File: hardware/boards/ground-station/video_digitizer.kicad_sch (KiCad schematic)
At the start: 9 parts, among them Y601 28.63636MHz

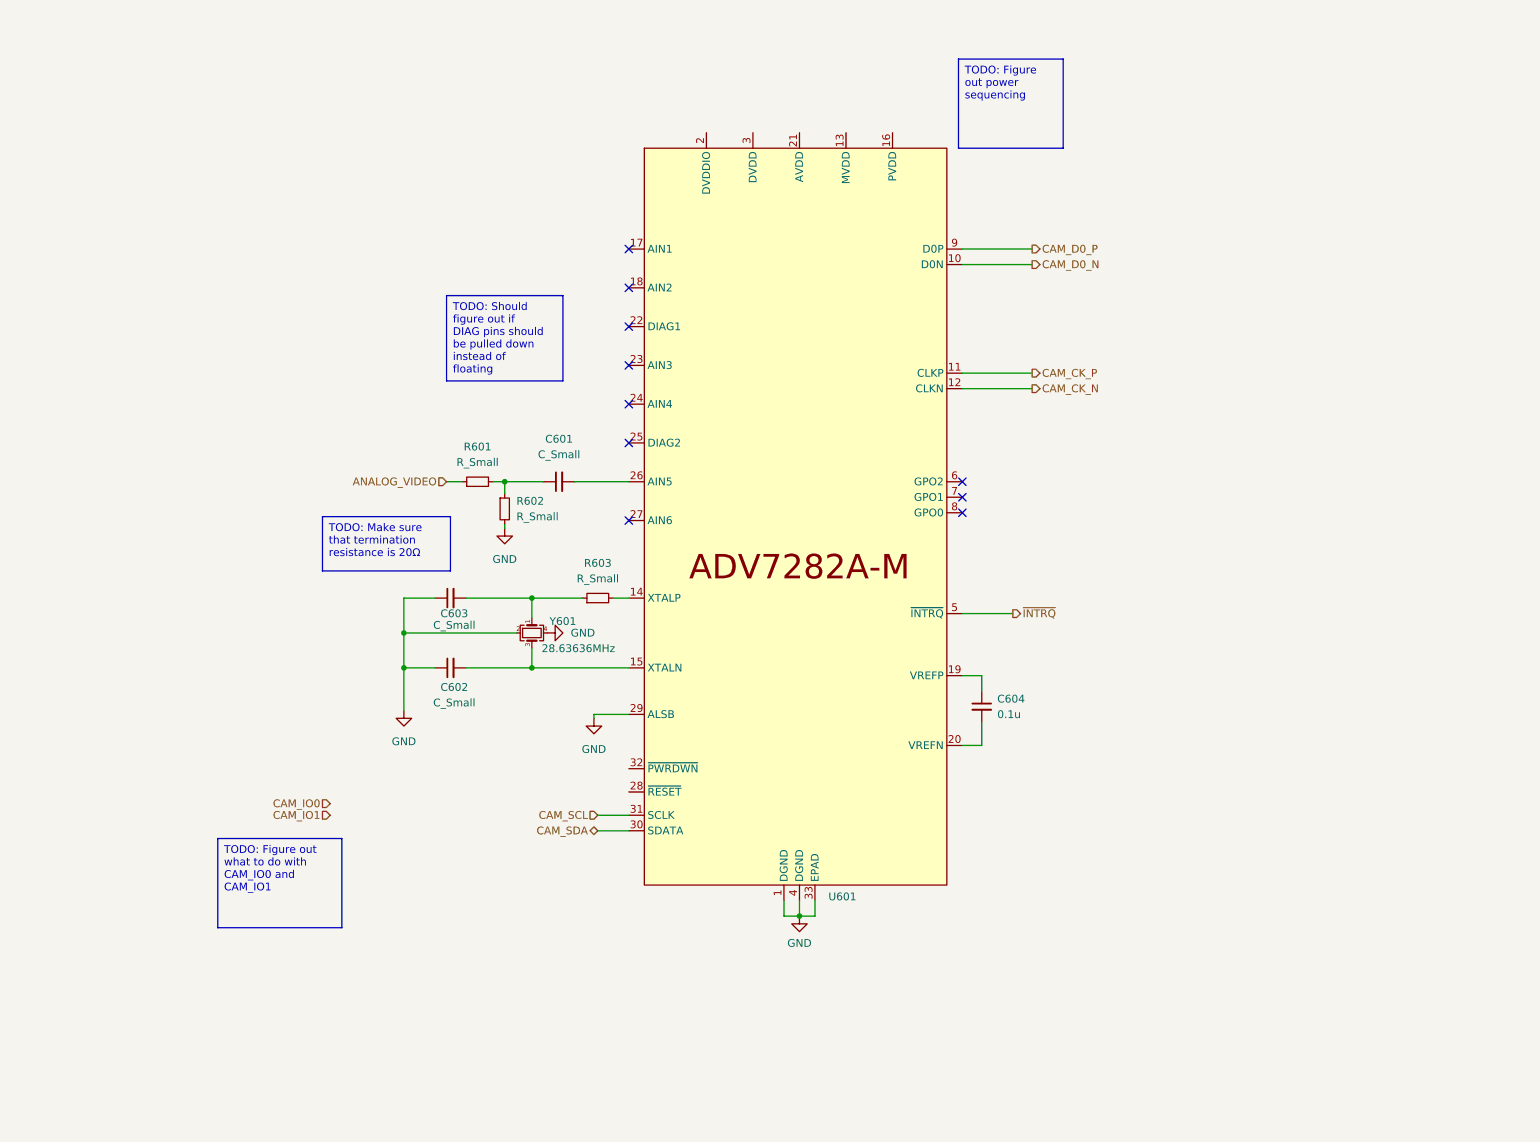
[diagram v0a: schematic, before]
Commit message: Added power supplies to digitizer IC
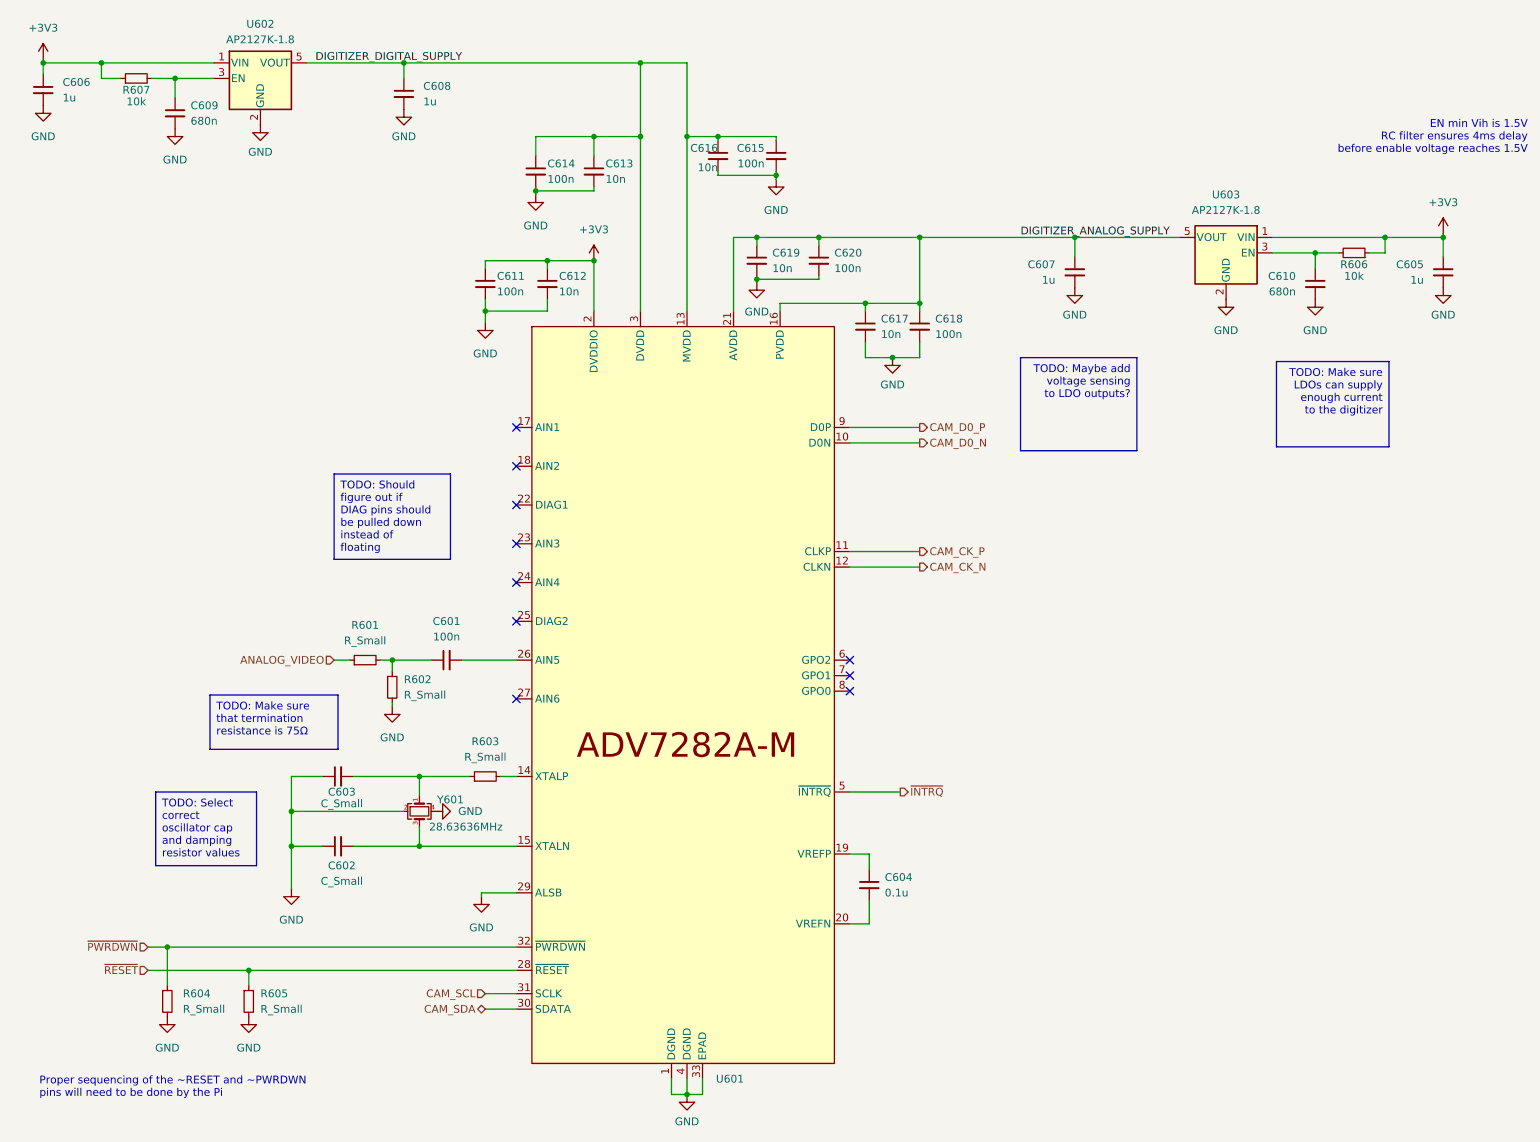
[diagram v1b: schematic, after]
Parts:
- added C605, C606, C607, C608: 1u, symbol Device:C_Small
- added C609, C610: 680n, symbol Device:C_Small
- added C611, C614, C615, C618, C620: 100n, symbol Device:C_Small
- added C612, C613, C616, C617, C619: 10n, symbol Device:C_Small
- added R604, R605: R_Small, symbol Device:R_Small
- added R606, R607: 10k, symbol Device:R_Small
- added U602, U603: AP2127K-1.8, Package_TO_SOT_SMD:SOT-23-5, symbol Regulator_Linear:AP2127K-1.8
- C601: value C_Small -> 100n
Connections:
- net GND: now also C605.2, C606.2, C607.2, C608.2, C609.2, C610.2, C611.2, C612.2, C613.2, C614.2, C615.2, C616.2, C617.2, C618.2, C619.2, C620.2, R604.2, R605.2, U602.2 (GND), U603.2 (GND)
- net DIGITIZER_DIGITAL_SUPPLY: now reaches U601.13 (MVDD)
- net DIGITIZER_DIGITAL_SUPPLY: now also U601.3 (DVDD), C608.1, C613.1, C614.1, C615.1, C616.1, U602.5 (VOUT)
- net DIGITIZER_ANALOG_SUPPLY: now reaches U601.16 (PVDD)
- net DIGITIZER_ANALOG_SUPPLY: now also U601.21 (AVDD), C607.1, C617.1, C618.1, C619.1, C620.1, U603.5 (VOUT)
- net +3V3: now reaches U601.2 (DVDDIO)
- net +3V3: now also C605.1, C606.1, C611.1, C612.1, R606.1, R607.1, U602.1 (VIN), U603.1 (VIN)
- net ~{RESET}: now reaches U601.28 (~{RESET})
- net ~{RESET}: now also R605.1
- net ~{PWRDWN}: now reaches U601.32 (~{PWRDWN})
- net ~{PWRDWN}: now also R604.1
- new net: C610.1, R606.2, U603.3 (EN)
- new net: C609.1, R607.2, U602.3 (EN)
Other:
- note added: "EN min Vih is 1.5V RC filter ensures 4ms delay before enable voltage reaches 1.5V"
- note added: "Proper sequencing of the ~RESET and ~PWRDWN pins will need to be done by the Pi"
- moved on the sheet: C601, C602, C603, C604, R601, R602, R603, Y601

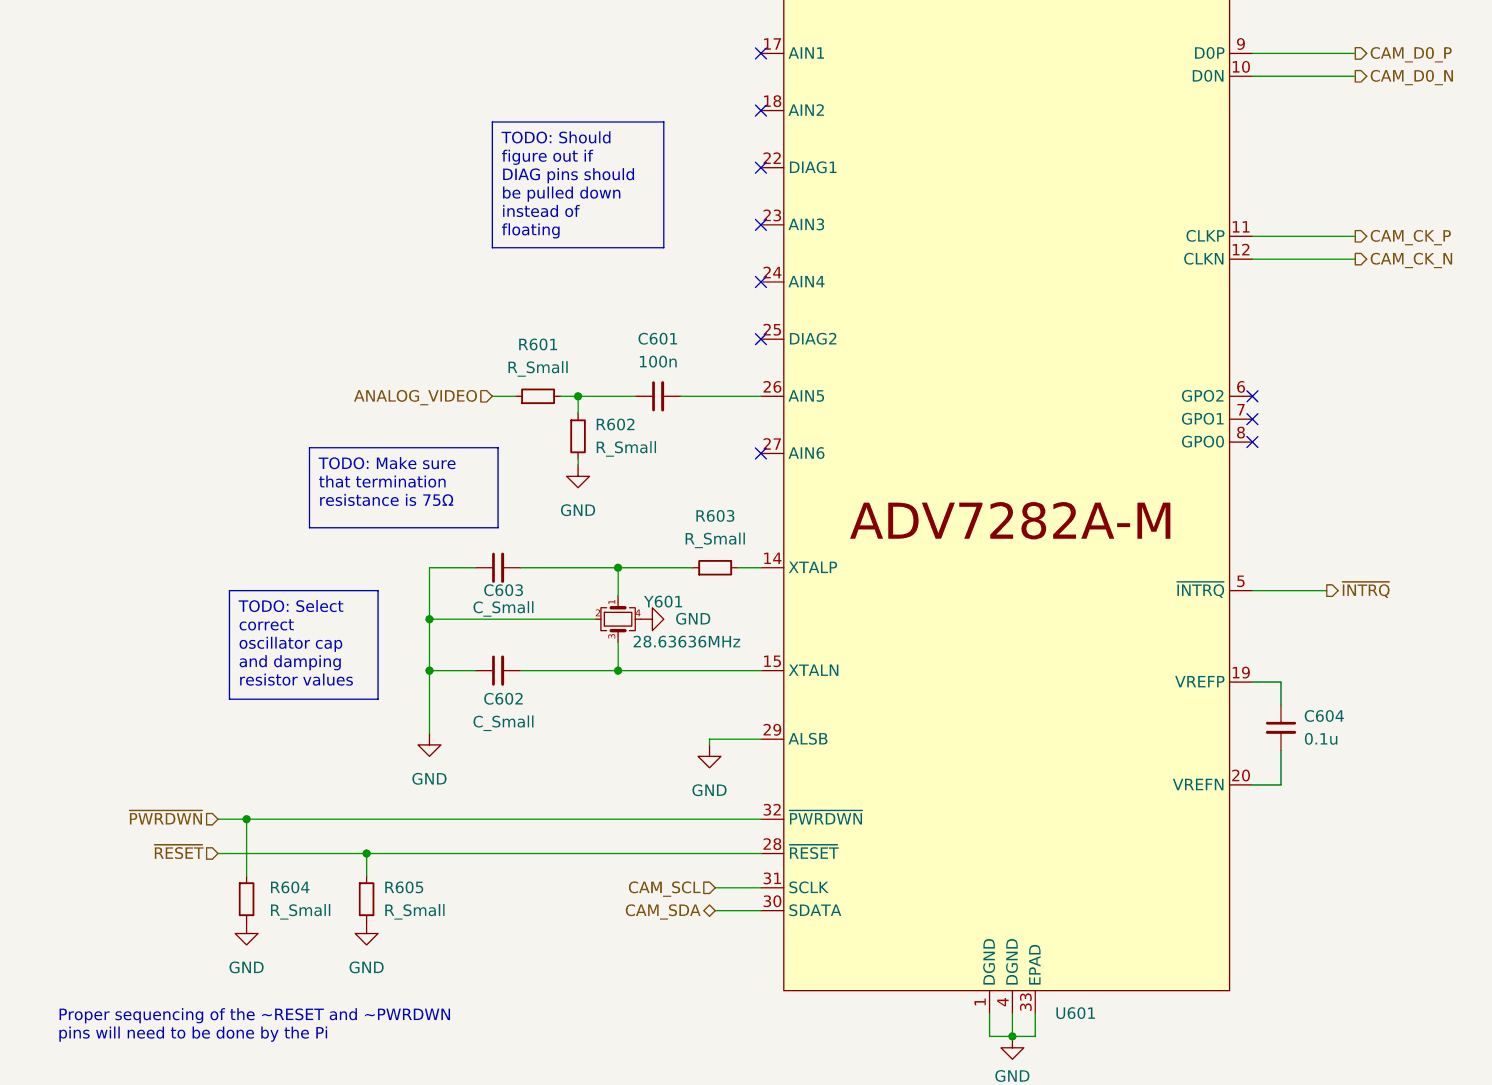
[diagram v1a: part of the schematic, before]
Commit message: Added oscillator to video digitizer
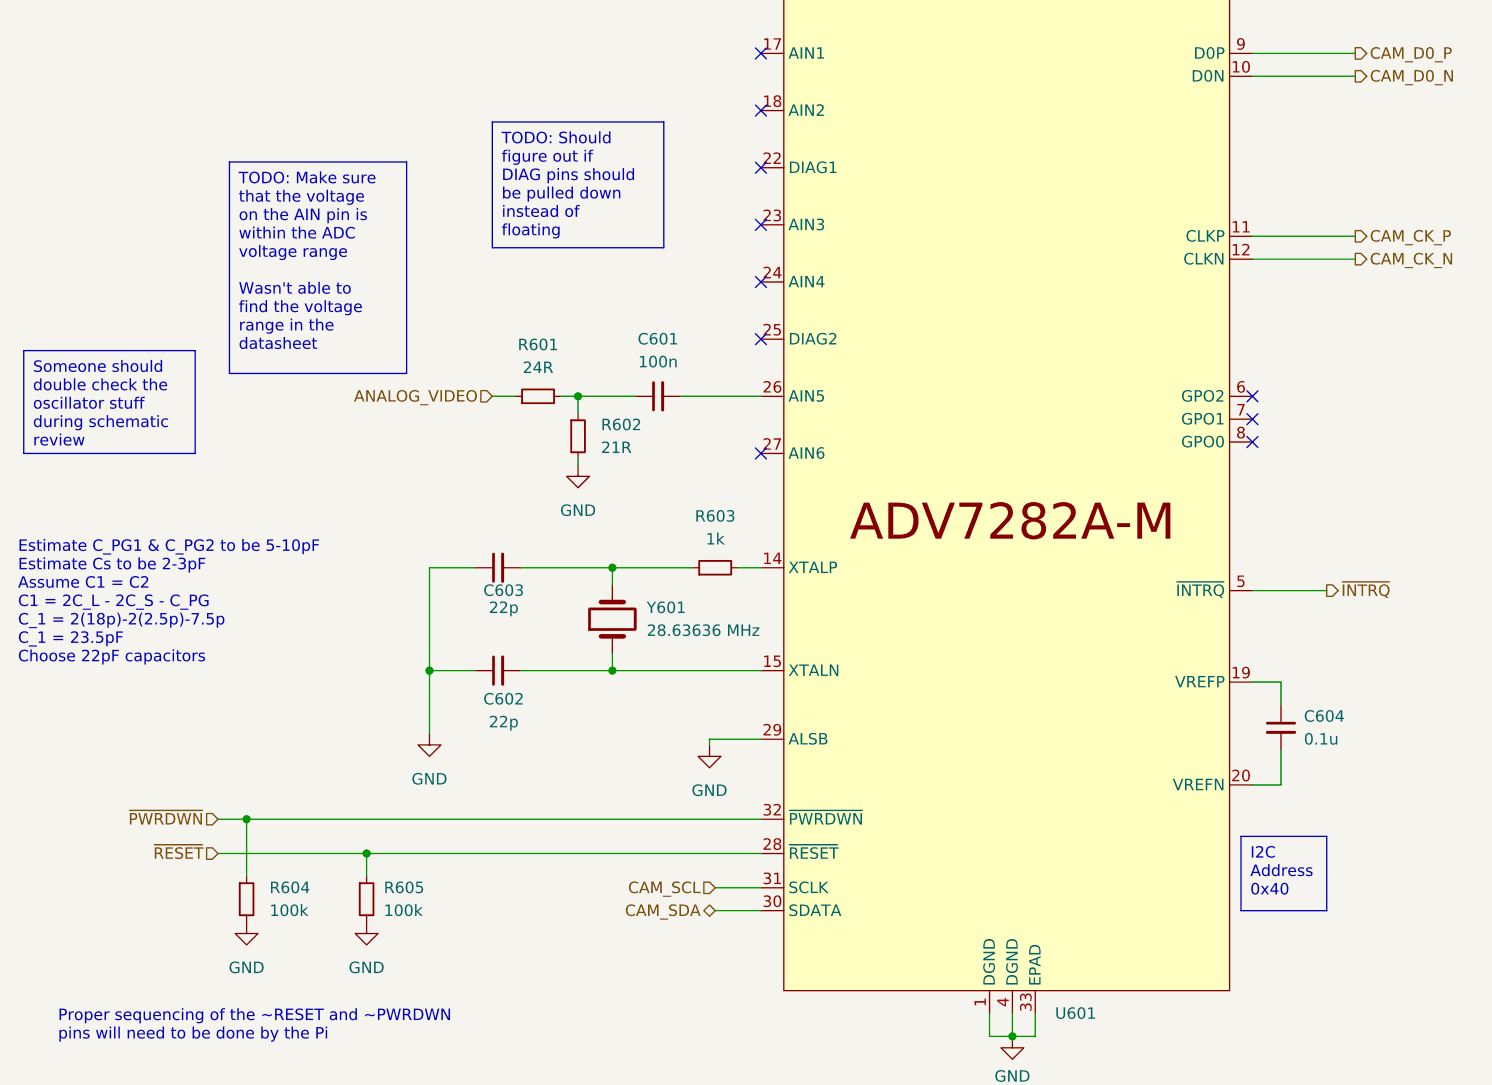
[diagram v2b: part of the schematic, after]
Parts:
- removed Y601: 28.63636MHz, symbol Device:Crystal_GND24_Small
- added Y601: 28.63636 MHz, symbol Device:Crystal
- C602, C603: value C_Small -> 22p
- R601: value R_Small -> 24R
- R602: value R_Small -> 21R
- R603: value R_Small -> 1k
- R604, R605: value R_Small -> 100k
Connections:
- net at C603.2, R603.1: now also Y601.2
- net at C602.2, U601.15 (XTALN): now also Y601.1
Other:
- note added: "Estimate C_PG1 & C_PG2 to be 5-10pF Estimate Cs to be 2-3pF Assume C1 = C2 C1 = 2C_L - 2C_S - C_PG C_1 = 2(18p)-2(2.5p)-7.5p C_1 = 23.5pF Choose 22pF capacitors"

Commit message: Updated video radio to RX5808
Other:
- title: (none) -> Video Digitizer
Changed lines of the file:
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@@
 (kicad_sch (version 20230121) (generator eeschema)
   (paper "A4")
+  (title_block
+    (title "Video Digitizer")
+  )
   (junction (at 81.28 147.955) (diameter 0) (color 0 0 0 0)
   )

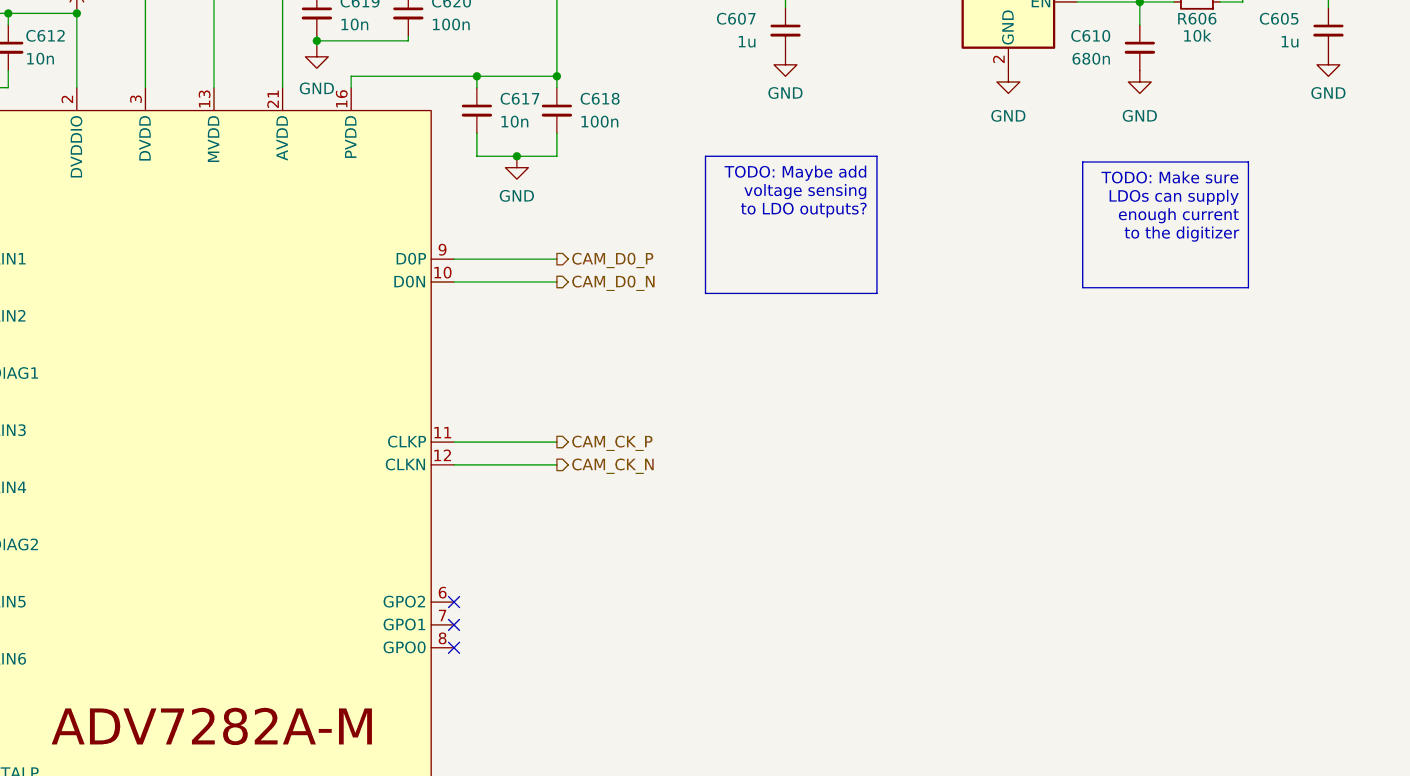
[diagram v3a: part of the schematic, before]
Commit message: Change board input power to 5V, add connector for OTS wireless power TX
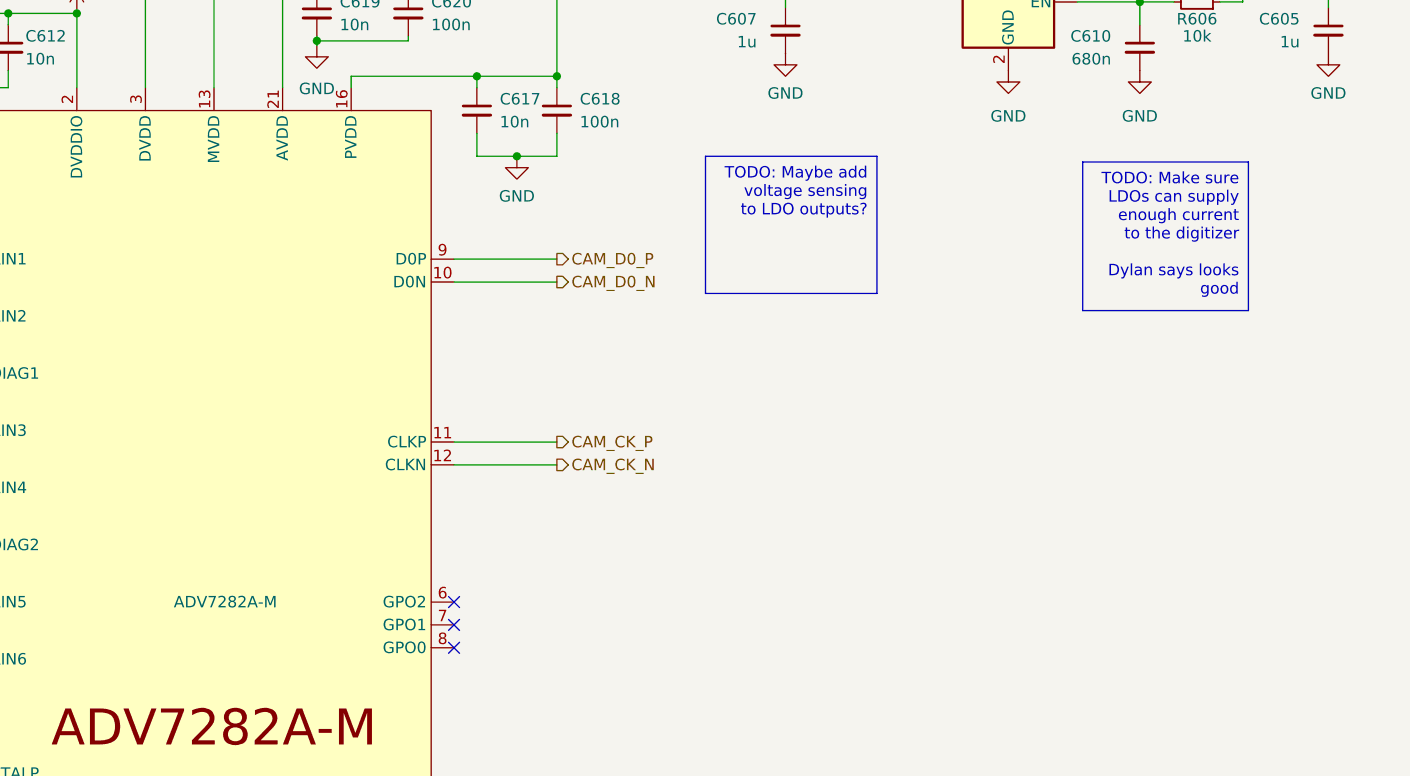
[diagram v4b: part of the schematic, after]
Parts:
- U601: value ~ -> ADV7282A-M
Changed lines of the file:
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@@
     )
   )
-  (text_box "TODO: Make sure LDOs can supply enough current to the digitizer"
-    (at 222.25 68.58 0) (size 18.415 13.97)
+  (text_box "TODO: Make sure LDOs can supply enough current to the digitizer\n\nDylan says looks good"
+    (at 222.25 68.58 0) (size 18.415 16.51)
     (stroke (width 0) (type default))
     (fill (type color) (color 255 255 0 1))
@@
       (effects (font (size 1.27 1.27)) (justify left))
     )
-    (property "Value" "~" (at 127 117.475 0)
+    (property "Value" "ADV7282A-M" (at 127 117.475 0)
       (effects (font (size 1.27 1.27)))
     )
@@
       (effects (font (size 1.27 1.27)) hide)
     )
-    (property "Datasheet" "" (at 127 117.475 0)
-      (effects (font (size 1.27 1.27)) hide)
-    )
+    (property "Datasheet" "https://www.analog.com/media/en/technical-documentation/data-sheets/adv7282a.pdf" (at 127 117.475 0)
+      (effects (font (size 1.27 1.27)) hide)
+    )
